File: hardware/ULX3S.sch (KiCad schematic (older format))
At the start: 5 parts, among them J2 VS_SCL, J6 HS_SDA, J8 DE_IRQ

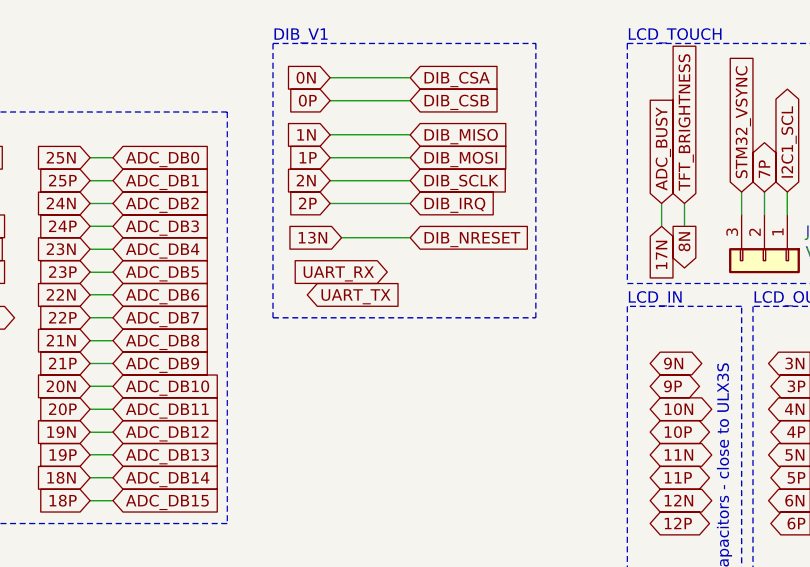
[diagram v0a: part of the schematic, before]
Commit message: Before AGND - GND
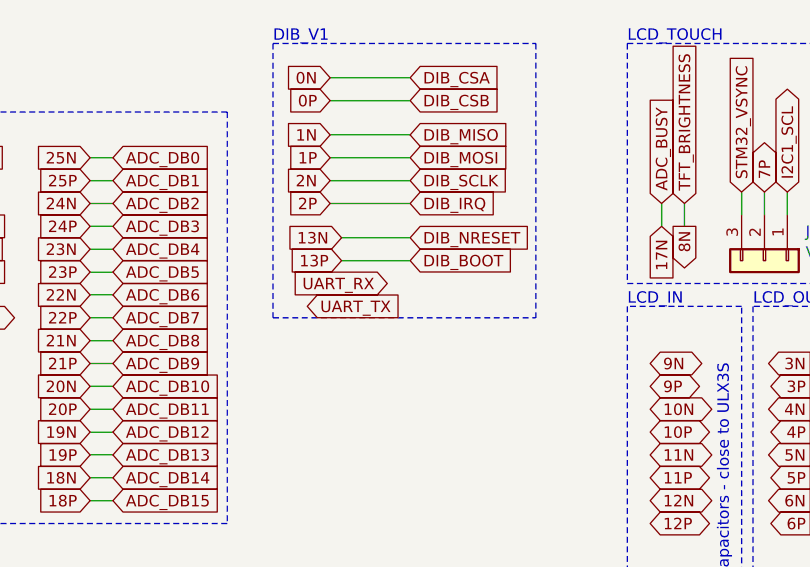
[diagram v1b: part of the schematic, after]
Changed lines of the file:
@@
 Text GLabel 6350 2050 2    50   Input ~ 0
 DIB_NRESET
-Text GLabel 6250 2200 0    50   Input ~ 0
+Text GLabel 6250 2250 0    50   Input ~ 0
 UART_RX
-Text GLabel 5900 2300 2    50   Input ~ 0
+Text GLabel 5900 2350 2    50   Input ~ 0
 UART_TX
 Text Notes 5750 1200 0    50   ~ 0
@@
 Wire Wire Line
 	4200 3600 4200 3700
+Text GLabel 6350 2150 2    50   Input ~ 0
+DIB_BOOT
+Text GLabel 6050 2150 0    50   Input ~ 0
+13P
+Wire Wire Line
+	6050 2150 6350 2150
 $EndSCHEMATC

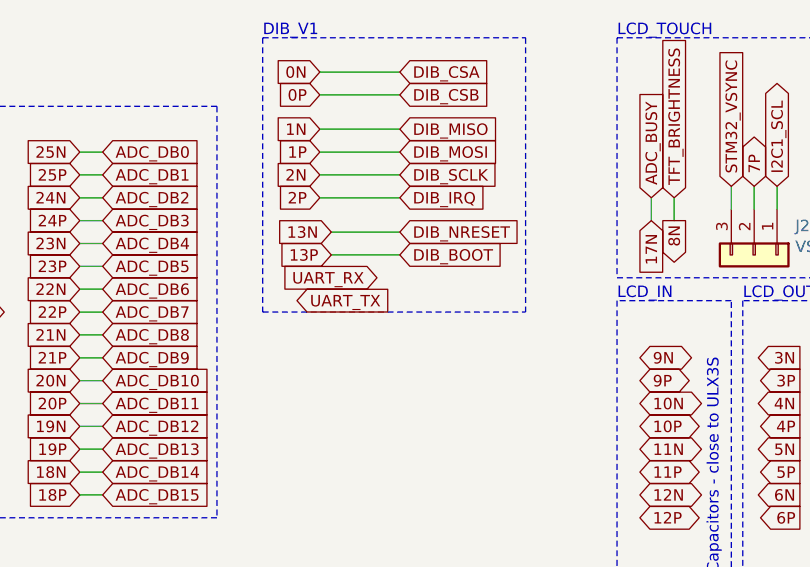
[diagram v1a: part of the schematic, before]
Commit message: Finishing routing
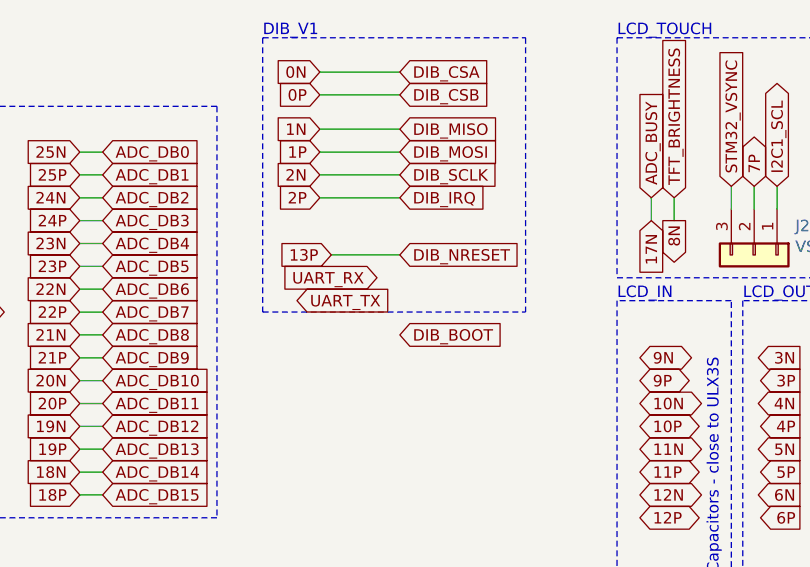
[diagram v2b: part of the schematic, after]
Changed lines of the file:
@@
 Text GLabel 6350 1900 2    50   Input ~ 0
 DIB_IRQ
-Text GLabel 6350 2050 2    50   Input ~ 0
+Text GLabel 6350 2150 2    50   Input ~ 0
 DIB_NRESET
 Text GLabel 6250 2250 0    50   Input ~ 0
@@
 Text GLabel 6000 1900 0    50   Input ~ 0
 2P
-Text GLabel 6050 2050 0    50   Input ~ 0
-13N
 Wire Wire Line
 	6000 1350 6350 1350
@@
 Wire Wire Line
 	6000 1800 6350 1800
-Wire Wire Line
-	6050 2050 6350 2050
 Wire Wire Line
 	6000 1900 6350 1900
@@
 Wire Wire Line
 	4200 3600 4200 3700
-Text GLabel 6350 2150 2    50   Input ~ 0
+Text GLabel 6350 2500 2    50   Input ~ 0
 DIB_BOOT
 Text GLabel 6050 2150 0    50   Input ~ 0
